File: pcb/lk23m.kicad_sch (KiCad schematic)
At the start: 59 parts, among them J1 Conn_01x02, SW1 RotaryEncoder_Switch_MP, SW10 SW_Push, SW11 SW_Push, SW12 SW_Push, SW13 SW_Push, SW14 SW_Push, SW15 SW_Push, SW16 SW_Push, SW17 SW_Push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

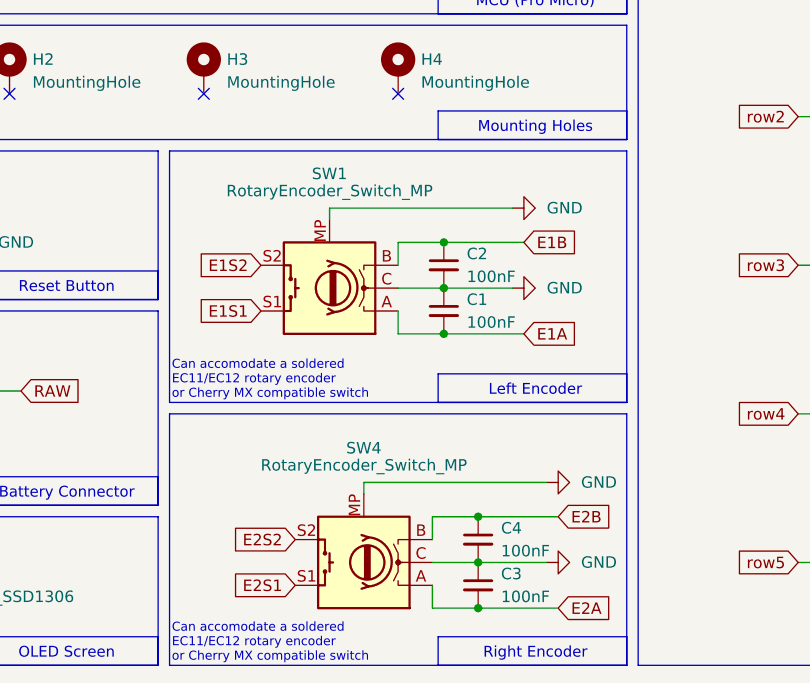
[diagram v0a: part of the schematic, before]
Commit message: Model should be done, we should just look at exporting keyboard.pretty as a library
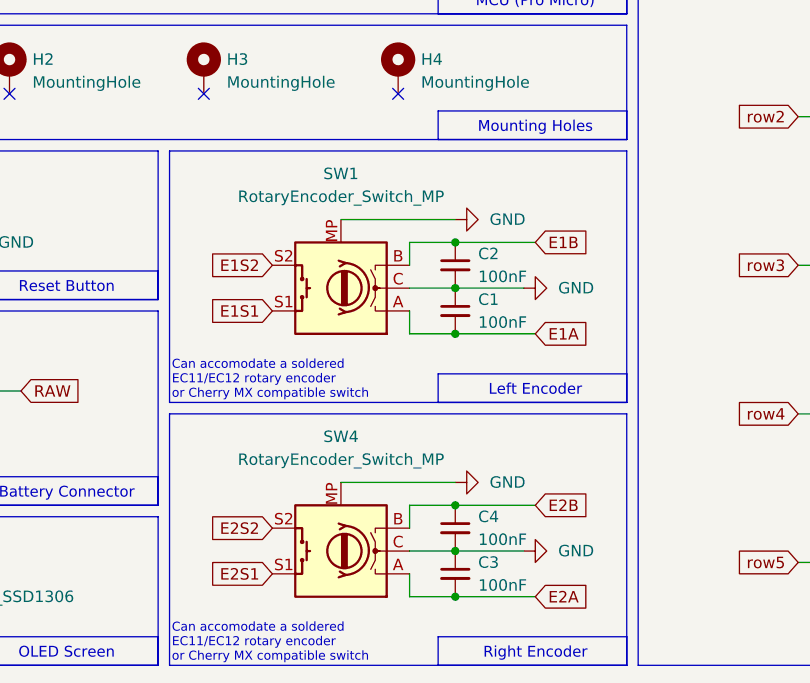
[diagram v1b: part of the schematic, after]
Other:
- moved on the sheet: C1, C2, C3, C4, SW1, SW4

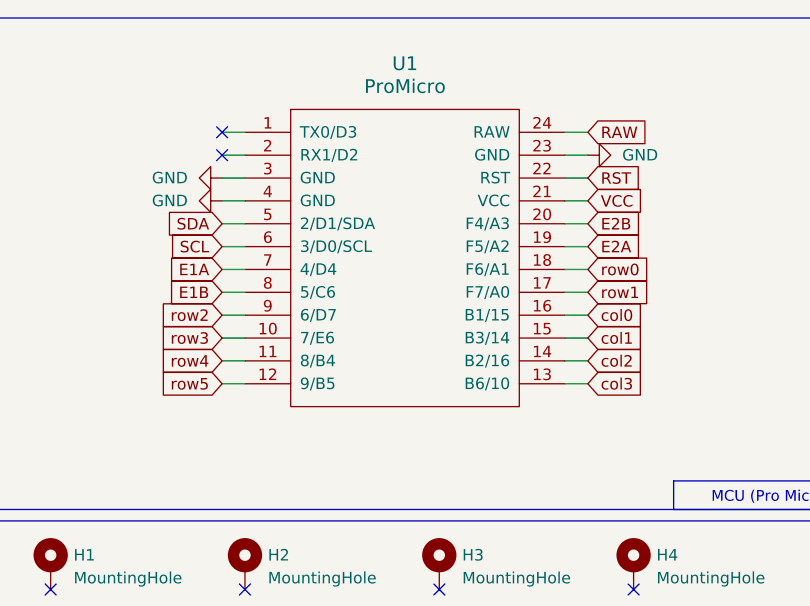
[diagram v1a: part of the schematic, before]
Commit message: Migrate to using symbols and footprints from gtihub.com/lambdakb/kicad-lkbd
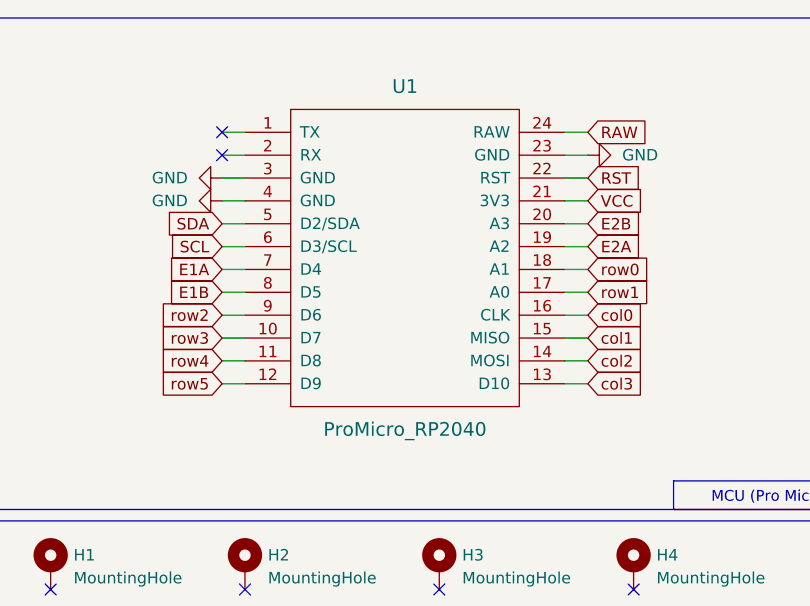
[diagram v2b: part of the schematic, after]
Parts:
- C1, C2, C3, C4: footprint keyboard:Capacitor_SMD+THT_1206_5.0x2.5mm_P5.00mm -> LKBD_Common:Capacitor_SMD+THT_1206_5.0x2.5mm_P5.00mm
- D1, D10, D11, D12, D13, D14, D15, D16, D17, D18, D19, D2, D20, D21, D22, D23, D3, D4, D5, D6, D7, D8, D9: footprint keyboard:Diode_SMD+THT_SOD123_DO35_P7.62mm -> LKBD_Common:Diode_SMD+THT_SOD123_DO35_P7.62mm
- OL1: footprint keyboard:OLED_SSD1306_128x32_0.91inch_I2C_btmSilk -> LKBD_OLED:OLED_SSD1306_128x32_0.91inch_I2C_btmSilk
- SW1, SW4: footprint keyboard:SW_MX_EC11_THT_sqSilk -> LKBD_KeySwitch:SW_MX_EC11_THT_sqSilk
- SW10, SW11, SW12, SW13, SW14, SW15, SW16, SW17, SW18, SW19, SW20, SW21, SW22, SW5, SW6, SW7, SW8, SW9: footprint keyboard:SW_MX_HotSwap_THT_sqSilk -> LKBD_KeySwitch:SW_MX_HotSwap_THT_sqSilk
- SW2, SW3: footprint keyboard:SW_MX_THT_sqSilk -> LKBD_KeySwitch:SW_MX_THT_sqSilk
- SW23: footprint keyboard:SW_MX_2U_HotSwap_THT_sqSilk -> LKBD_KeySwitch:SW_MX_2U_HotSwap_THT_sqSilk
- U1: value ProMicro -> ProMicro_RP2040; footprint keyboard:MCU_KB2040_DIP-24_Socket_Reverse -> LKBD_MCU:MCU_KB2040_DIP-24_Socket_Reverse; symbol kbd:ProMicro -> LKBD_MCU:ProMicro_RP2040

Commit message: Fix SMD footprint position + add kibot setup
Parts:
- C1, C2, C3, C4: LCSC (none) -> C24497
- D1, D10, D11, D12, D13, D14, D15, D16, D17, D18, D19, D2, D20, D21, D22, D23, D3, D4, D5, D6, D7, D8, D9: footprint LKBD_Common:Diode_SMD+THT_SOD123_DO35_P7.62mm -> LKBD_Common:Diode_SMD+THT_SOD123_DO35_P6.5mm; LCSC (none) -> C2128
- SW24: footprint Button_Switch_THT:SW_PUSH_1P1T_6x3.5mm_H4.3_APEM_MJTP1243 -> LKBD_Common:SW_PUSH_1P1T_6x3.5mm
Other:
- company: (none) -> LambdaKB.dev
- title: (none) -> LK23M

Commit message: Move KiBot config to reusable folder and fix PCBDraw output
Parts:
- C1, C2, C3, C4: JLC (none) -> 1206
- D1, D10, D11, D12, D13, D14, D15, D16, D17, D18, D19, D2, D20, D21, D22, D23, D3, D4, D5, D6, D7, D8, D9: JLC (none) -> SOD-323; LCSC C2128 -> C81598
- SW10, SW11, SW12, SW13, SW14, SW15, SW16, SW17, SW18, SW19, SW20, SW21, SW22, SW23, SW5, SW6, SW7, SW8, SW9: JLC (none) -> SMD,14.5x5.9mm; JLCPosOffset (none) -> 0.635,3.81; LCSC (none) -> C41430893
- SW25: JLC (none) -> SMD; LCSC (none) -> C221841
